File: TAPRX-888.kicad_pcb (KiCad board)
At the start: 6 copper layers, 83.5 x 99.4 mm, 225 parts, among them J1 CONN_SMA_JACK_EDGE_JLC_With_N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, J10 U.FL-R, J11 Conn_JTAG10-mini, J2 CONN_SMA_JACK_EDGE_JLC_With_N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, J3 CONN_SMA_JACK_EDGE_JLC_With_N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, J4 CONN_SMA_JACK_EDGE_JLC_With_N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, J5 USB-3.0, J6 Conn_01x03, J7 Conn_01x03, J8 Conn_01x03, J9 Conn_01x03, Q1 PMOS Si2343DS, Q2 MMBT3904, Q3 PMOS Si2343DS, U1 AP2114H-3.3TRG1, U10 XO-19.2MHZ, U11 CYUSB3014-BZXCT, U14 LP5907MFX-3.3, U16 TLV3501, U18 NC7SV157, U19 74LVC2G14, U2 AP2114H-3.3TRG1, U20 Si5351A, U21 NC7SV157, U22 SN65LVDS1, U3 AP2114H-3.3TRG1, U4 LP5907MFX-3.3, U5 UMW AMS1117-1.2, U6 AD8370, U7 TVS-SP3011, U8 LTC2208CUP#PBF, U9 MX25L3233FM2I, X1 TCXO-27M

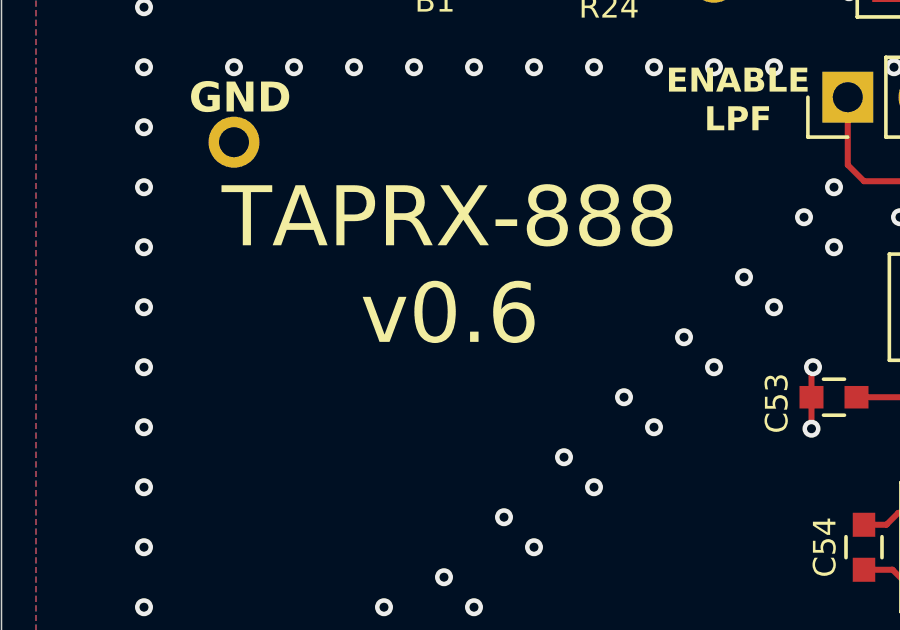
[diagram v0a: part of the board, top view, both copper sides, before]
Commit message: Track release rev on PCB silkscreen; set 0.6 baseline
The PCB silkscreen version was a hardcoded "TAPRX-888 v0.6" on both silk
layers -- static board art that didn't track the release, so it read v0.6
while the release lane was at v0.5. The designer's number (v0.6) is the
correct one, so the release lane was mis-seeded one behind.

- TAPRX-888.kicad_pcb: silkscreen version -> "TAPRX-888 v${REVISION}" on F.SilkS
  and B.SilkS, so CI stamps the actual release rev at build time (like the
  existing "Commit: ${GIT_HASH}" silk). Renders "vDEV" on a local open.
- dev-release.yml: seed the pre-release baseline at v0.6 (was 0.5).
- VERSION.txt / RELEASE_STRATEGY.md: reflect the v0.6 baseline.

This is a design change, so merging it cuts the next pre-release (v0.6), whose
gerbers will silkscreen "v0.6" -- matching tag, silk, and the designer's intent.

Co-Authored-By: Claude Opus 4.8 <noreply@anthropic.com>
Claude-Session: https://claude.ai/code/session_019A4jkTeNPLki8CdfTWEUwM
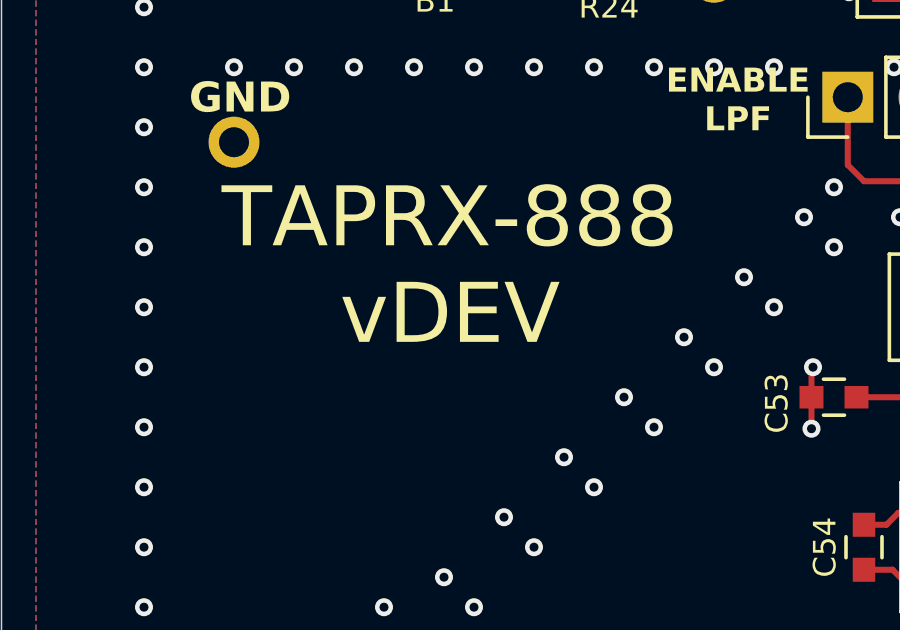
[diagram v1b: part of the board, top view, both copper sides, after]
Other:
- board text added: "TAPRX-888 v${REVISION}"
- board text removed: "TAPRX-888 v0.6"
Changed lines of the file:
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@@
 		)
 	)
-	(gr_text "TAPRX-888\nv0.6"
+	(gr_text "TAPRX-888\nv${REVISION}"
 		(at 111.2 98.4 0)
 		(layer "F.SilkS")
@@
 		)
 	)
-	(gr_text "TAPRX-888\nv0.6"
+	(gr_text "TAPRX-888\nv${REVISION}"
 		(at 111 98.4 0)
 		(layer "B.SilkS")
